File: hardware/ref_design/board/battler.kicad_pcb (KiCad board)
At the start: 2 copper layers, 0 parts

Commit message: Reference design: board routed and DRC clean
- Core copy made faithful: Raspberry Pi's 0402 land patterns for the core
  passives (tools/lib_from_ref.py), their 3V3 stubs into the pour under the
  chip kept, and the uncopied-pad check made layer-aware (their board has a
  second flash footprint on the back, which had cost every QSPI track).
- TPS63001 re-placed and its power loop drawn by route.py as TI's layout
  guidance asks.
- tools/maze.py: a small A* router for the flash's SD2 line and for any
  connection Freerouting leaves open, with bounded rip-up.
- route.py: order-stable pre-routes (so --reuse is valid), fiducial
  keep-outs for the router, a second Freerouting pass when needed with a
  watchdog for its warning dialog, loose-copper cleanup.

check_pcb.py: 0 errors, 0 unconnected, 0 schematic parity issues.

Co-Authored-By: Claude Opus 5.5 (1M context) <noreply@anthropic.com>
Claude-Session: https://claude.ai/code/session_01KGgEu3CbFtCsvHRQgAFiCN
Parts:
- added C1: 10u, Capacitor_SMD:C_0603_1608Metric, F.Cu at (128.0, 111.2)
- added C10: 100n, battler:C_0402_1005Metric_RPi, F.Cu at (117.2, 80.2)
- added C11: 100n, battler:C_0402_1005Metric_RPi, F.Cu at (108.8, 83.0)
- added C12: 100n, battler:C_0402_1005Metric_RPi, F.Cu at (91.7, 82.7)
- added C13: 100n, battler:C_0402_1005Metric_RPi, F.Cu at (108.1, 78.2)
- added C14: 100n, battler:C_0402_1005Metric_RPi, F.Cu at (102.9, 76.0)
- added C15: 100n, battler:C_0402_1005Metric_RPi, F.Cu at (99.5, 92.0)
- added C16: 100n, battler:C_0402_1005Metric_RPi, F.Cu at (97.8, 76.0)
- added C17: 100n, battler:C_0402_1005Metric_RPi, F.Cu at (95.5, 91.5)
- added C18: 100n, battler:C_0402_1005Metric_RPi, F.Cu at (104.3, 91.5)
- added C19: 100n, battler:C_0402_1005Metric_RPi, F.Cu at (93.3, 79.3)
- added C2: 4.7u, Capacitor_SMD:C_0603_1608Metric, F.Cu at (134.0, 118.0)
- added C20: 100n, battler:C_0402_1005Metric_RPi, F.Cu at (100.2, 76.0)
- added C21: 100n, battler:C_0402_1005Metric_RPi, F.Cu at (91.7, 85.4)
- added C22: 100n, battler:C_0402_1005Metric_RPi, F.Cu at (100.5, 92.0)
- added C23: 10u, Capacitor_SMD:C_0603_1608Metric, F.Cu at (111.0, 93.0)
- added C24: 4.7u, battler:C_0402_1005Metric_RPi_Wide, F.Cu at (106.1, 87.0)
- added C25: 4.7u, battler:C_0402_1005Metric_RPi_Wide, F.Cu at (107.0, 87.0)
- added C26: 4.7u, battler:C_0402_1005Metric_RPi, F.Cu at (106.5, 89.2)
- added C27: 15p, battler:C_0402_1005Metric_RPi, F.Cu at (89.6, 82.6)
- added C28: 15p, battler:C_0402_1005Metric_RPi, F.Cu at (89.6, 85.6)
- added C29: 1u, Capacitor_SMD:C_0402_1005Metric, F.Cu at (92.0, 104.8)
- added C3: 4.7u, Capacitor_SMD:C_0603_1608Metric, F.Cu at (131.4, 118.4)
- added C30: 100n, Capacitor_SMD:C_0402_1005Metric, F.Cu at (92.0, 106.0)
- added C31: 4.7u, Capacitor_SMD:C_0603_1608Metric, F.Cu at (71.4, 117.6)
- added C32: 1u, Capacitor_SMD:C_0603_1608Metric, F.Cu at (67.2, 131.8)
- added C33: 220n, Capacitor_SMD:C_0402_1005Metric, F.Cu at (71.6, 121.4)
- added C34: 10u, Capacitor_SMD:C_0603_1608Metric, F.Cu at (97.0, 59.0)
- added C35: 100n, Capacitor_SMD:C_0402_1005Metric, F.Cu at (100.2, 59.0)
- added C4: 100n, Capacitor_SMD:C_0402_1005Metric, F.Cu at (132.4, 121.2)
- added C5: 10u, Capacitor_SMD:C_0603_1608Metric, F.Cu at (133.9, 126.2)
- added C6: 10u, Capacitor_SMD:C_0603_1608Metric, F.Cu at (128.3, 125.0)
- added C7: 10u, Capacitor_SMD:C_0603_1608Metric, F.Cu at (128.3, 128.0)
- added C8: 100n, Capacitor_SMD:C_0402_1005Metric, F.Cu at (106.8, 96.6)
- added D1: amber, LED_SMD:LED_0603_1608Metric, F.Cu at (131.2, 88.0)
- added D2: BAT54C, Package_TO_SOT_SMD:SOT-23, F.Cu at (131.6, 70.2)
- added D3: BAT54WS, Diode_SMD:D_SOD-323, F.Cu at (131.8, 73.4)
- added D4: red, LED_SMD:LED_0603_1608Metric, F.Cu at (131.2, 92.0)
- added D5: B5819WS, Diode_SMD:D_SOD-323, F.Cu at (69.6, 129.2)
- added FB1: 120R@100MHz, Inductor_SMD:L_0603_1608Metric, F.Cu at (104.4, 62.8)
- added FB2: 120R@100MHz, Inductor_SMD:L_0603_1608Metric, F.Cu at (106.2, 62.8)
- added FID1: Fiducial, Fiducial:Fiducial_1mm_Mask2mm, F.Cu at (67.3, 71.0)
- added FID2: Fiducial, Fiducial:Fiducial_1mm_Mask2mm, F.Cu at (133.2, 141.6)
- added FID3: Fiducial, Fiducial:Fiducial_1mm_Mask2mm, F.Cu at (66.8, 141.6)
- added H1: M2, MountingHole:MountingHole_2.2mm_M2, F.Cu at (131.4, 64.0)
- added H2: M2, MountingHole:MountingHole_2.2mm_M2, F.Cu at (68.6, 64.0)
- added H3: M2, MountingHole:MountingHole_2.2mm_M2, F.Cu at (131.4, 136.0)
- added H4: M2, MountingHole:MountingHole_2.2mm_M2, F.Cu at (68.6, 136.0)
- added H5: M2, MountingHole:MountingHole_2.2mm_M2, F.Cu at (100.0, 38.9)
- added H6: M2, MountingHole:MountingHole_2.2mm_M2, F.Cu at (100.0, 161.1)
- added J1: TYPE-C-31-M-12, battler:USB_C_Receptacle_HRO_TYPE-C-31-M-12, F.Cu at (132.9, 100.0)
- added J2: S2B-PH-SM4-TB, battler:JST_PH_S2B-PH-SM4-TB_1x02-1MP_P2.00mm_Horizontal, F.Cu at (100.0, 152.3)
- added J3: FH35C-39S-0.3SHW(50), battler:Hirose_FH35C-39S-0.3SHW_1x39-1MP_P0.30mm_Horizontal, F.Cu at (94.6, 110.5)
- added J4: SPEAKER, battler:Speaker_Wire_Pads_P4.0mm, B.Cu at (100.0, 57.5)
- added J5: SWD, battler:JST_SH_SM03B-SRSS-TB_1x03-1MP_P1.00mm_Horizontal, F.Cu at (68.3, 102.0)
- added J6: UART, battler:JST_SH_SM03B-SRSS-TB_1x03-1MP_P1.00mm_Horizontal, F.Cu at (68.3, 112.0)
- added L1: 2.2u, Inductor_SMD:L_1008_2520Metric, F.Cu at (131.2, 127.3)
- added L2: 3.3u, battler:AOTA-B201610S3R3-101-T, F.Cu at (108.7, 87.0)
- added L3: 10u, Inductor_SMD:L_1008_2520Metric, F.Cu at (69.4, 125.6)
- added Q1: 2N7002, Package_TO_SOT_SMD:SOT-23, F.Cu at (129.6, 81.8)
- added R1: 5.1k, Resistor_SMD:R_0402_1005Metric, F.Cu at (126.0, 97.4)
- added R10: 100k, Resistor_SMD:R_0402_1005Metric, F.Cu at (124.2, 109.6)
- added R11: 1k, Resistor_SMD:R_0402_1005Metric, F.Cu at (128.6, 88.0)
- added R12: 100, Resistor_SMD:R_0402_1005Metric, F.Cu at (130.0, 121.2)
- added R13: 100k, Resistor_SMD:R_0402_1005Metric, F.Cu at (128.4, 70.0)
- added R14: 10k, Resistor_SMD:R_0402_1005Metric, F.Cu at (128.4, 73.4)
- added R15: 100k, Resistor_SMD:R_0402_1005Metric, F.Cu at (134.0, 70.2)
- added R16: 100k, Resistor_SMD:R_0402_1005Metric, F.Cu at (132.4, 83.8)
- added R17: 470k, Resistor_SMD:R_0402_1005Metric, F.Cu at (104.0, 96.6)
- added R18: 470k, Resistor_SMD:R_0402_1005Metric, F.Cu at (105.4, 96.6)
- added R19: 33, battler:R_0402_1005Metric_RPi, F.Cu at (108.3, 89.2)
- added R2: 5.1k, Resistor_SMD:R_0402_1005Metric, F.Cu at (126.0, 102.6)
- added R20: 1k, battler:R_0402_1005Metric_RPi, F.Cu at (91.7, 84.2)
- added R21: 27, battler:R_0402_1005Metric_RPi, F.Cu at (108.8, 84.0)
- added R22: 27, battler:R_0402_1005Metric_RPi, F.Cu at (108.8, 85.0)
- added R23: 10k, battler:R_0402_1005Metric_RPi, F.Cu at (117.7, 76.4)
- added R24: 0, battler:R_0402_1005Metric_RPi, F.Cu at (117.2, 72.6)
- added R25: 1k, battler:R_0402_1005Metric_RPi, F.Cu at (118.6, 72.6)
- added R26: 1k, Resistor_SMD:R_0402_1005Metric, F.Cu at (71.8, 91.0)
- added R27: 1k, Resistor_SMD:R_0402_1005Metric, F.Cu at (128.6, 92.0)
- added R28: 33, Resistor_SMD:R_0402_1005Metric, F.Cu at (97.6, 96.6)
- added R29: 33, Resistor_SMD:R_0402_1005Metric, F.Cu at (99.1, 96.6)
- added R3: 10k, Resistor_SMD:R_0402_1005Metric, F.Cu at (124.0, 97.4)
- added R30: 3.6, Resistor_SMD:R_0603_1608Metric, F.Cu at (71.6, 131.8)
- added R31: 100k, Resistor_SMD:R_0402_1005Metric, F.Cu at (67.0, 117.6)
- added R32: 47k, Resistor_SMD:R_0402_1005Metric, F.Cu at (95.4, 63.4)
- added R4: 10k, Resistor_SMD:R_0402_1005Metric, F.Cu at (124.0, 102.6)
- added R5: 1.2k, Resistor_SMD:R_0402_1005Metric, F.Cu at (128.2, 113.9)
- added R6: 1.2k, Resistor_SMD:R_0402_1005Metric, F.Cu at (128.2, 116.2)
- added R7: 100k, Resistor_SMD:R_0402_1005Metric, F.Cu at (124.2, 112.0)
- added R8: 100k, Resistor_SMD:R_0402_1005Metric, F.Cu at (125.4, 112.0)
- added R9: 100k, Resistor_SMD:R_0402_1005Metric, F.Cu at (126.6, 112.0)
- added RT1: 10k B3380, Resistor_SMD:R_0603_1608Metric, F.Cu at (110.0, 128.0)
- added SW1: P1 UP, battler:DSL_button_4ring, F.Cu at (79.3, 154.1)
- added SW10: P2 DOWN, battler:DSL_button_4ring, F.Cu at (120.7, 31.9)
- added SW11: P2 LEFT, battler:DSL_button_4ring, F.Cu at (127.7, 38.9)
- added SW12: P2 RIGHT, battler:DSL_button_4ring, F.Cu at (113.7, 38.9)
- added SW13: P2 A, battler:DSL_button_4ring, F.Cu at (71.8, 38.9)
- added SW14: P2 B, battler:DSL_button_4ring, F.Cu at (79.3, 31.4)
- added SW15: P2 X, battler:DSL_button_4ring, F.Cu at (79.3, 46.4)
- added SW16: P2 Y, battler:DSL_button_4ring, F.Cu at (86.8, 38.9)
- added SW17: PWR, battler:SW_Alps_SKRTLAE010_Pullback, F.Cu at (133.2, 78.0)
- added SW18: BOOTSEL, battler:SW_SPST_TS-1088-xR020, F.Cu at (68.8, 80.0)
- added SW19: RESET, battler:SW_SPST_TS-1088-xR020, F.Cu at (68.8, 88.0)
- added SW2: P1 DOWN, battler:DSL_button_4ring, F.Cu at (79.3, 168.1)
- added SW3: P1 LEFT, battler:DSL_button_4ring, F.Cu at (72.3, 161.1)
- added SW4: P1 RIGHT, battler:DSL_button_4ring, F.Cu at (86.3, 161.1)
- added SW5: P1 A, battler:DSL_button_4ring, F.Cu at (128.2, 161.1)
- added SW6: P1 B, battler:DSL_button_4ring, F.Cu at (120.7, 168.6)
- added SW7: P1 X, battler:DSL_button_4ring, F.Cu at (120.7, 153.6)
- added SW8: P1 Y, battler:DSL_button_4ring, F.Cu at (113.2, 161.1)
- added SW9: P2 UP, battler:DSL_button_4ring, F.Cu at (120.7, 45.9)
- added TP1: VBUS, TestPoint:TestPoint_Pad_D1.0mm, B.Cu at (92.0, 53.0)
- added TP2: VSYS, TestPoint:TestPoint_Pad_D1.0mm, B.Cu at (96.0, 53.0)
- added TP3: VBAT, TestPoint:TestPoint_Pad_D1.0mm, B.Cu at (100.0, 53.0)
- added TP4: +3V3, TestPoint:TestPoint_Pad_D1.0mm, B.Cu at (104.0, 53.0)
- added TP5: GND, TestPoint:TestPoint_Pad_D1.0mm, B.Cu at (108.0, 53.0)
- added U1: USBLC6-2SC6, Package_TO_SOT_SMD:SOT-23-6, F.Cu at (130.6, 107.6)
- added U2: BQ24074RGTR, Package_DFN_QFN:VQFN-16-1EP_3x3mm_P0.5mm_EP1.6x1.6mm_ThermalVias, F.Cu at (131.4, 114.6)
- added U3: TPS63001DRCR, Package_SON:Texas_DRC0010J_ThermalVias, F.Cu at (131.2, 123.8)
- added U4: RP2350B, battler:RP2350B_QFN80_RPi, F.Cu at (100.0, 84.0)
- added U5: W25Q128JVPIQ, Package_SON:WSON-8-1EP_6x5mm_P1.27mm_EP3.4x4.3mm, F.Cu at (112.8, 77.0)
- added U6: TPS61160DRVR, Package_SON:WSON-6-1EP_2x2mm_P0.65mm_EP1x1.6mm_ThermalVias, F.Cu at (69.2, 121.0)
- added U7: MAX98357AETE+T, Package_DFN_QFN:TQFN-16-1EP_3x3mm_P0.5mm_EP1.23x1.23mm_ThermalVias, F.Cu at (100.0, 63.0)
- added X1: 12MHz, battler:ABM8-272-T3, F.Cu at (86.0, 84.0)
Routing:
- net VSYS: track 0.00 -> 211.7 mm, vias 0 -> 6
- net VBAT: track 0.00 -> 196.2 mm, vias 0 -> 3
- net P1_B: track 0.00 -> 132.6 mm, vias 0 -> 2
- net P1_X: track 0.00 -> 125.9 mm, vias 0 -> 2
- net P1_Y: track 0.00 -> 120.5 mm, vias 0 -> 2
- net GND: track 0.00 -> 117.0 mm, vias 0 -> 334
- net P1_A: track 0.00 -> 108.3 mm, vias 0 -> 2
- net VBUS: track 0.00 -> 101.6 mm, vias 0 -> 2
- net P1_DOWN: track 0.00 -> 93.6 mm
- net P1_LEFT: track 0.00 -> 88.2 mm, vias 0 -> 2
- net CHG_STAT_N: track 0.00 -> 86.3 mm, vias 0 -> 4
- net P1_RIGHT: track 0.00 -> 83.1 mm, vias 0 -> 2
- net P1_UP: track 0.00 -> 80.3 mm
- net /Power/PWR_EN: track 0.00 -> 78.8 mm, vias 0 -> 2
- net UART_RX: track 0.00 -> 73.1 mm, vias 0 -> 2
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- added copper zone on F.Cu, net +1V1
- added copper zone on F.Cu, net +3V3
- added copper zone on In2.Cu, net +3V3
- added copper zone on B.Cu, net GND
- added copper zone on F.Cu, net GND
- added copper zone on In1.Cu, net GND
- added copper zone on F.Cu, net VREG_LX
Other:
- board outline added: 70.4 x 151.2 mm
- copper layers 2 -> 4
- rule pad_to_mask_clearance: 0.05 -> 0

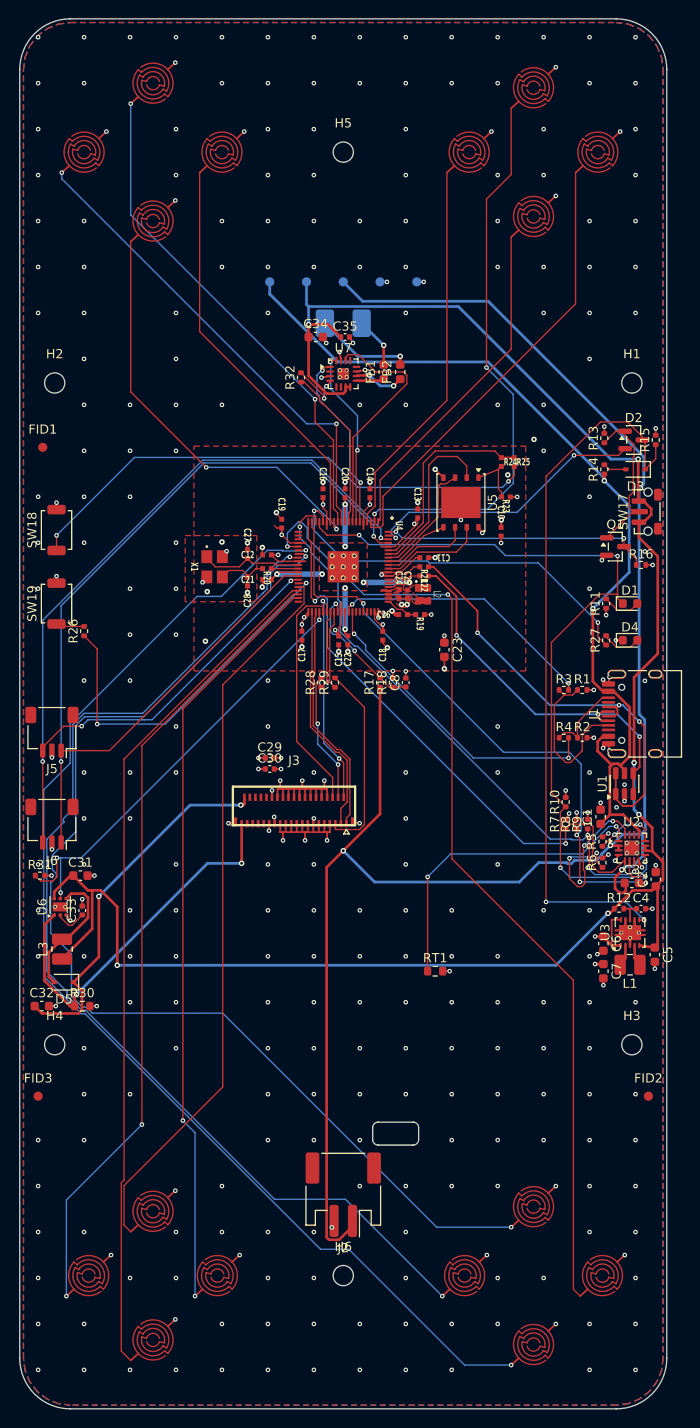
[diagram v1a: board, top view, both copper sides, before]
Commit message: Reference design: QD3525 panel, fab outputs, fit check
The $25-35 Displaytech DT035 is replaced by the QD3525, a bare 3.5in IPS
ST7796U panel of the same class at about $5-8 with a published drawing
and pinout (the panel inside LCDwiki's MSP3525 module).

- J3 is now the landing for its 48-contact solder tail (tools/fp_panel.py),
  wired as the maker's module wires it; TE goes to GPIO32.
- Backlight: an AP3156 charge pump drives each of the six parallel LEDs
  through its own current sink, set over one GPIO (BL_SDI). Its symbol
  comes from tools/sym_lib.py (Konnect's create_symbol draws no body).
- case.scad is built around a fixed panel bay, so the board outline,
  buttons and screws stay put; the lid, lens and STLs follow the panel.
- Routing: fan-out vias kept off pads, the AP3156's GND pins stubbed into
  its thermal pad, loose copper trimmed at the end; silk.py re-runnable.
- fab/: gerbers and drill, JLC BOM (40 part numbers) and CPL (91
  placements), STEP, renders, schematic and assembly PDFs.

check_netlist: PASS. ERC: 0 errors. DRC: 0 errors, 0 unconnected,
0 parity issues (2 cosmetic silk warnings at the USB-C). check_fit: PASS.

Co-Authored-By: Claude Opus 5.5 (1M context) <noreply@anthropic.com>
Claude-Session: https://claude.ai/code/session_01KGgEu3CbFtCsvHRQgAFiCN
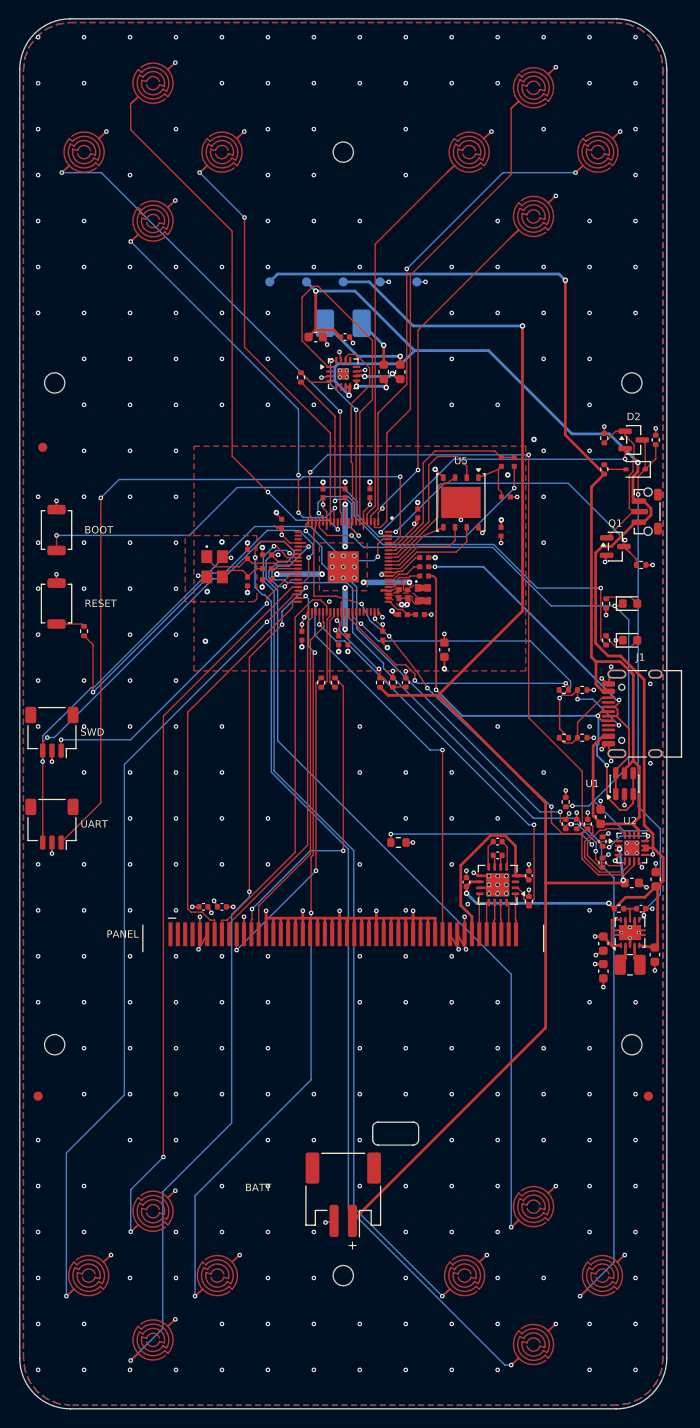
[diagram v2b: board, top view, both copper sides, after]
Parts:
- removed D5: B5819WS, Diode_SMD:D_SOD-323
- removed L3: 10u, Inductor_SMD:L_1008_2520Metric
- removed R30: 3.6, Resistor_SMD:R_0603_1608Metric
- added C36: 1u, Capacitor_SMD:C_0402_1005Metric, F.Cu at (116.8, 113.9)
- C31: value 4.7u -> 1u; footprint Capacitor_SMD:C_0603_1608Metric -> Capacitor_SMD:C_0402_1005Metric
- C32: footprint Capacitor_SMD:C_0603_1608Metric -> Capacitor_SMD:C_0402_1005Metric
- C33: value 220n -> 1u
- J3: value FH35C-39S-0.3SHW(50) -> QD3525; footprint battler:Hirose_FH35C-39S-0.3SHW_1x39-1MP_P0.30mm_Horizontal -> battler:QD3525_FPC_1x48_P0.80mm_Solder
- U6: value TPS61160DRVR -> AP3156FVG-7; footprint Package_SON:WSON-6-1EP_2x2mm_P0.65mm_EP1x1.6mm_ThermalVias -> Package_DFN_QFN:QFN-16-1EP_4x4mm_P0.65mm_EP2.5x2.5mm_ThermalVias
- moved C32 54.9 mm to (120.2, 117.6), turned to 90 degrees
- moved R31 53.3 mm to (120.2, 120.4), turned to 90 degrees
- moved U6 47.7 mm to (116.8, 118.6), turned to 180 degrees
- moved C33 45.6 mm to (116.8, 115.4), turned to 180 degrees
- moved C31 42.0 mm to (113.4, 118.3), turned to 90 degrees
- moved C29 17.7 mm to (84.8, 121.0)
- moved C30 15.9 mm to (86.8, 121.0)
- moved RT1 14.6 mm to (106.0, 114.0)
- moved J3 14.5 mm to (100.0, 124.0)
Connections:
- C33 pad 1: /Display/BL_COMP -> /Display/BL_C1P
- C33 pad 2: GND -> /Display/BL_C1N
- J3 pad 1: LCD_RST -> (no net)
- J3 pad 10: GND -> /Display/LCD_SCK
- J3 pad 11: GND -> +3V3
- J3 pad 12: GND -> /Display/LCD_MOSI
- J3 pad 13: GND -> LCD_MISO
- J3 pad 2: LCD_CS -> (no net)
- J3 pad 27: +3V3 -> GND
- J3 pad 28: +3V3 -> GND
- J3 pad 3: LCD_DC -> (no net)
- J3 pad 30: (no net) -> GND
- J3 pad 31: (no net) -> GND
- J3 pad 32: (no net) -> GND
- J3 pad 33: (no net) -> GND
- J3 pad 34: (no net) -> GND
- J3 pad 35: (no net) -> GND
- J3 pad 36: (no net) -> GND
- J3 pad 37: (no net) -> GND
- J3 pad 38: /Display/LED_A -> LCD_RST
- J3 pad 39: /Display/LED_K -> +3V3
- J3 pad 4: /Display/LCD_SCK -> (no net)
- J3 pad 5: /Display/LCD_MOSI -> +3V3
- J3 pad 6: LCD_MISO -> +3V3
- J3 pad 7: GND -> LCD_TE
- J3 pad 8: GND -> LCD_CS
- J3 pad 9: GND -> LCD_DC
- R31 pad 1: BL_PWM -> BL_SDI
- U4 pad 40: (no net) -> LCD_TE
- U4 pad 44: BL_PWM -> BL_SDI
- U6 pad 1: /Display/LED_K -> /Display/LED_K6
- U6 pad 2: /Display/BL_COMP -> BL_SDI
- U6 pad 3: GND -> (no net)
- U6 pad 4: /Display/BL_SW -> /Display/LED_A
- U6 pad 5: BL_PWM -> /Display/BL_C2P
- U6 pad 6: VSYS -> /Display/BL_C1P
- U6 pad 7: GND -> /Display/BL_C1N
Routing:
- net VSYS: track 211.7 -> 157.3 mm, vias 6 -> 5
- net BL_PWM: track 49.5 -> 0.00 mm, vias 3 -> 0
- net BL_SDI: track 0.00 -> 45.4 mm, vias 0 -> 2
- net LCD_TE: track 0.00 -> 43.7 mm
- net /Display/LED_K: track 41.6 -> 0.00 mm, vias 2 -> 0
- net VBAT: track 196.2 -> 156.0 mm
- net P1_X: track 125.9 -> 88.8 mm
- net GND: track 117.0 -> 153.9 mm, vias 334 -> 355
- net P1_Y: track 120.5 -> 94.5 mm
- net P1_B: track 132.6 -> 107.5 mm
- net /Power/PWR_EN: track 78.8 -> 57.8 mm
- net /Display/LCD_SCK: track 14.2 -> 35.1 mm
- net I2S_DIN: track 19.8 -> 39.9 mm, vias 2 -> 0
- net LCD_CS: track 23.6 -> 43.2 mm, vias 2 -> 0
- net /Display/LED_A: track 40.2 -> 21.2 mm, vias 2 -> 0
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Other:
- board text added: "+"
- board text added: "3V3"
- board text added: "4 LAYERS 1.6 MM ENIG"
- board text added: "BATT"
- board text added: "BOOT"
- board text added: "GND"
- board text added: "PANEL"
- board text added: "RESET"
- board text added: "REV 2026-09-24"
- board text added: "SPEAKER"
- board text added: "SWD"
- board text added: "TWO-PLAYER HANDHELD REF-A"
- board text added: "UART"
- board text added: "VBAT"
- board text added: "VBUS"
- board text added: "VSYS"
